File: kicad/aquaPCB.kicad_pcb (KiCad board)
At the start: 2 copper layers, 100 x 100 mm, 149 parts, among them J1 12V IN, J11 SSR G17, J12 SSR G22, J13 SSR G23, J14 SSR G27, J15 IN1, J16 IN2, J17 IN3, J18 IN4, J19 1-Wire 1, J2 Raspberry Pi, J22 I2C 1, J23 I2C 2, J24 Display, J25 pH probe, J26 Module, J27 AIN3, J4 OUT G18, J5 OUT G19, J6 OUT G12, J7 OUT G13, J8 OUT G16, J9 OUT G26, Q1 AOD4184A, Q10 AOD4185, Q2 AOD4184A, Q3 AOD4184A, Q4 AOD4184A, Q5 AOD4184A, Q6 AOD4184A, U1 TPS54360B, U2 AMS1117-3.3, U3 74HCT244D, U4 ULN2803A, U5 ADS1115IDGSR, U6 TLV9062IDR

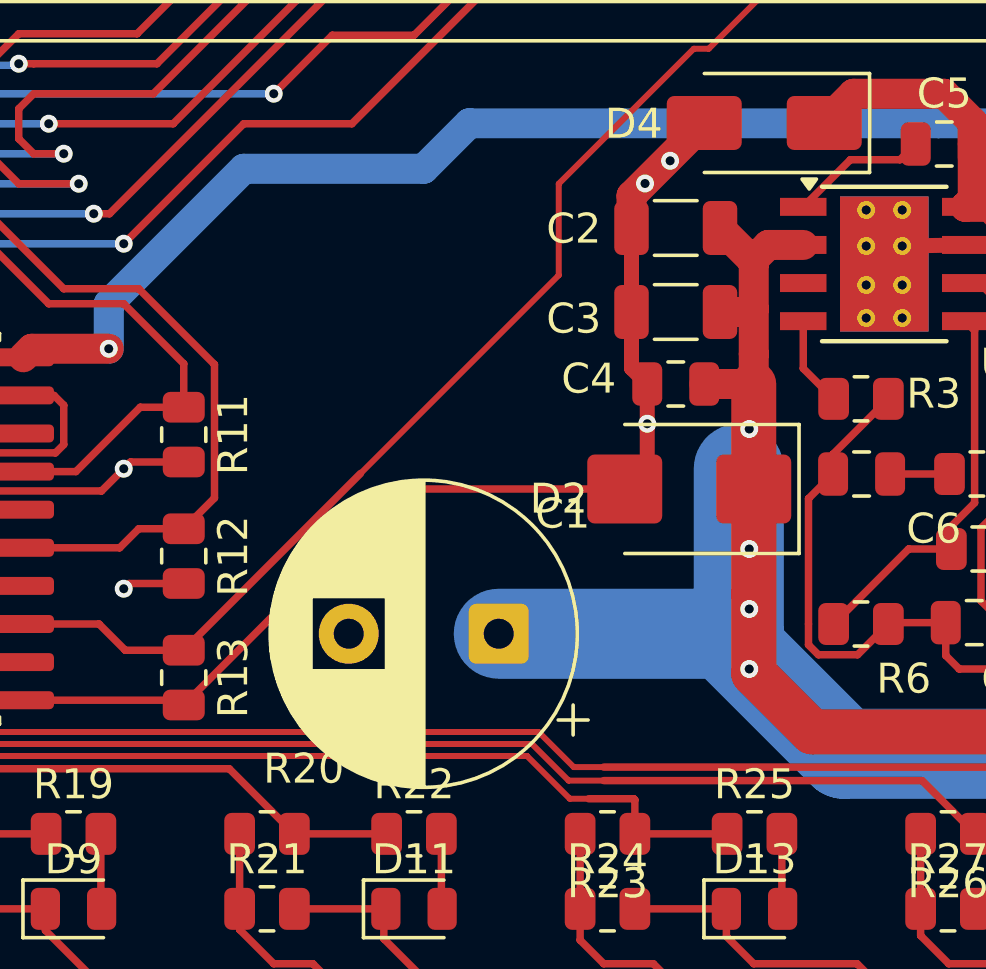
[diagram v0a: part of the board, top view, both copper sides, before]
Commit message: kicad: routing progress (by hand)
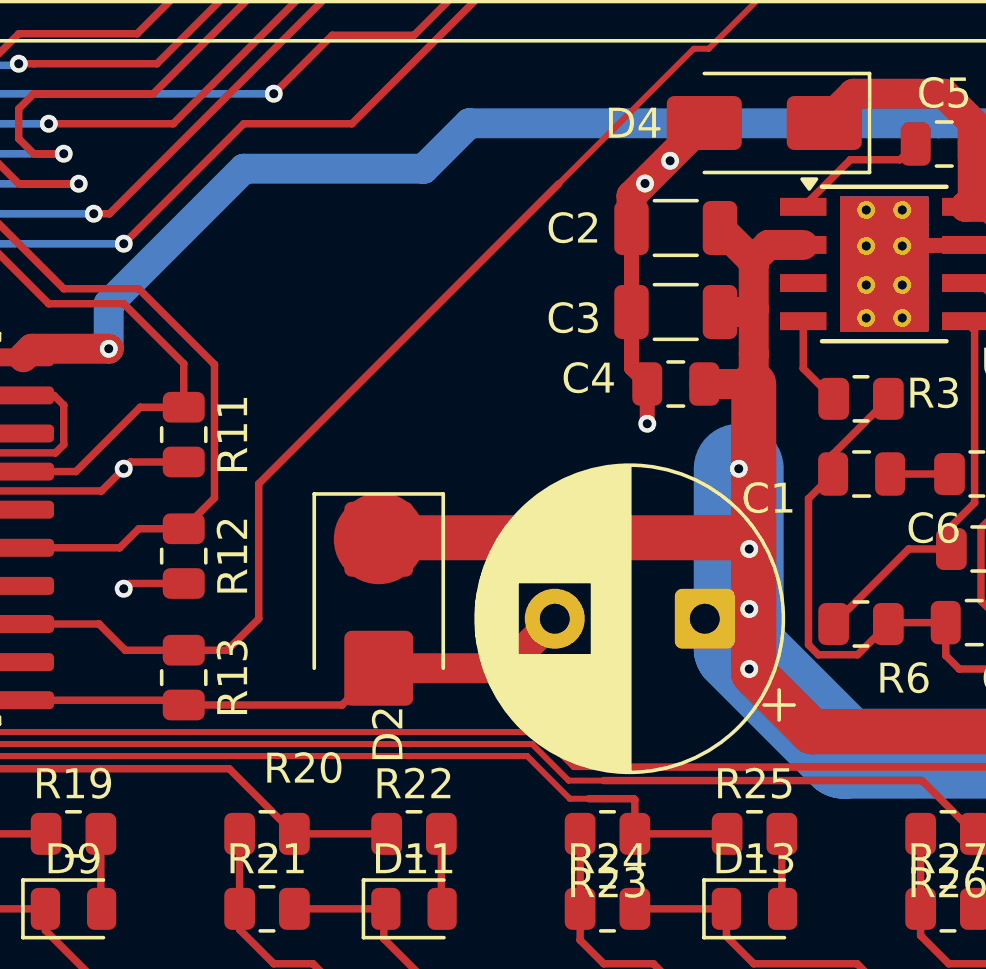
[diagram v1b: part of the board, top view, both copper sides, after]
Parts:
- moved D2 11.0 mm to (127.5, 98.5), turned to -90 degrees
- moved C1 6.89 mm to (138.4, 99.0)
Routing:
- net GND: track 441.3 -> 434.6 mm
- net VIN: track 365.2 -> 369.6 mm
- net GPIO18_Q1: track 37.6 -> 38.4 mm
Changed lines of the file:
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@@
 	(footprint "Diode_SMD:D_SMB"
 		(layer "F.Cu")
-		(at 137.85 94.675 180)
+		(at 127.5 98.5 -90)
 		(descr "Diode SMB (DO-214AA)")
 		(tags "Diode SMB (DO-214AA)")
 		(property "Reference" "D2"
-			(at 4.35 -0.325 0)
+			(at 4.35 -0.325 90)
 			(layer "F.SilkS")
 			(effects
@@
 		)
 		(property "Value" "SMBJ33A"
-			(at 0 3.1 0)
+			(at 0 3.1 90)
 			(layer "F.Fab")
 			(effects
@@
 		)
 		(property "Datasheet" ""
-			(at 0 0 180)
+			(at 0 0 270)
 			(unlocked yes)
 			(layer "F.Fab")
@@
 		)
 		(property "Description" "Zener diode"
-			(at 0 0 180)
+			(at 0 0 270)
 			(unlocked yes)
 			(layer "F.Fab")
@@
 		)
 		(property "LCSC" "C78419"
-			(at 0 0 180)
+			(at 0 0 270)
 			(unlocked yes)
 			(layer "F.Fab")
@@
 		(fp_line
 			(start -3.66 -2.15)
-			(end 2.15 -2.15)
+			(end -3.66 2.15)
 			(stroke
 				(width 0.12)
@@
 		(fp_line
 			(start -3.66 -2.15)
-			(end -3.66 2.15)
+			(end 2.15 -2.15)
 			(stroke
 				(width 0.12)
@@
 		)
 		(fp_line
-			(start 3.65 2.25)
-			(end -3.65 2.25)
+			(start -3.65 2.25)
+			(end -3.65 -2.25)
 			(stroke
 				(width 0.05)
@@
 		)
 		(fp_line
-			(start 3.65 -2.25)
-			(end 3.65 2.25)
+			(start 3.65 2.25)
+			(end -3.65 2.25)
 			(stroke
 				(width 0.05)
@@
 		)
 		(fp_line
-			(start -3.65 2.25)
-			(end -3.65 -2.25)
+			(start -3.65 -2.25)
+			(end 3.65 -2.25)
 			(stroke
 				(width 0.05)
@@
 		)
 		(fp_line
-			(start -3.65 -2.25)
-			(end 3.65 -2.25)
+			(start 3.65 -2.25)
+			(end 3.65 2.25)
 			(stroke
 				(width 0.05)
@@
 		)
 		(fp_line
-			(start 2.3 2)
-			(end -2.3 2)
+			(start -2.3 2)
+			(end -2.3 -2)
 			(stroke
 				(width 0.1)
@@
 		)
 		(fp_line
-			(start 2.3 -2)
-			(end 2.3 2)
+			(start 2.3 2)
+			(end -2.3 2)
 			(stroke
 				(width 0.1)
@@
 		)
 		(fp_line
-			(start 2.3 -2)
-			(end -2.3 -2)
+			(start 0.50118 0.75032)
+			(end 0.50118 -0.79908)
 			(stroke
 				(width 0.1)
@@
 		)
 		(fp_line
-			(start 0.50118 0.75032)
-			(end 0.50118 -0.79908)
+			(start -0.64944 0.00102)
+			(end 0.50118 0.75032)
 			(stroke
 				(width 0.1)
@@
 		)
 		(fp_line
-			(start 0.50118 0.00102)
-			(end 1.4994 0.00102)
+			(start -0.64944 0.00102)
+			(end -1.55114 0.00102)
 			(stroke
 				(width 0.1)
@@
 		(fp_line
 			(start -0.64944 0.00102)
-			(end 0.50118 0.75032)
+			(end 0.50118 -0.79908)
 			(stroke
 				(width 0.1)
@@
 		)
 		(fp_line
-			(start -0.64944 0.00102)
-			(end 0.50118 -0.79908)
+			(start 0.50118 0.00102)
+			(end 1.4994 0.00102)
 			(stroke
 				(width 0.1)
@@
 		)
 		(fp_line
-			(start -0.64944 0.00102)
-			(end -1.55114 0.00102)
+			(start -0.64944 -0.79908)
+			(end -0.64944 0.80112)
 			(stroke
 				(width 0.1)
@@
 		)
 		(fp_line
-			(start -0.64944 -0.79908)
-			(end -0.64944 0.80112)
+			(start 2.3 -2)
+			(end 2.3 2)
 			(stroke
 				(width 0.1)
@@
 		)
 		(fp_line
-			(start -2.3 2)
+			(start 2.3 -2)
 			(end -2.3 -2)
 			(stroke
@@
 		)
 		(fp_text user "${REFERENCE}"
-			(at 0 -3 0)
+			(at 0 -3 90)
 			(layer "F.Fab")
 			(effects
@@
 		)
 		(pad "1" smd roundrect
-			(at -2.15 0 180)
+			(at -2.15 0 270)
 			(size 2.5 2.3)
 			(layers "F.Cu" "F.Mask" "F.Paste")
@@
 		)
 		(pad "2" smd roundrect
-			(at 2.15 0 180)
+			(at 2.15 0 270)
 			(size 2.5 2.3)
 			(layers "F.Cu" "F.Mask" "F.Paste")
@@
 	(footprint "Capacitor_THT:CP_Radial_D10.0mm_P5.00mm"
 		(layer "F.Cu")
-		(at 131.5 99.5 180)
+		(at 138.367677 99 180)
 		(descr "CP, Radial series, Radial, pin pitch=5.00mm, diameter=10mm, height=16mm, Electrolytic Capacitor")
 		(tags "CP Radial series Radial pin pitch 5.00mm diameter 10mm height 16mm Electrolytic Capacitor")
@@
 	)
 	(segment
-		(start 136.45 93.925)
-		(end 135.7 94.675)
-		(width 0.5)
-		(layer "F.Cu")
-		(net "GND")
-	)
-	(segment
 		(start 150.7951 51.675)
 		(end 152.1 50.3701)
@@
 	)
 	(segment
+		(start 127.5 100.65)
+		(end 131.717677 100.65)
+		(width 1)
+		(layer "F.Cu")
+		(net "GND")
+	)
+	(segment
 		(start 125.4076 51.245)
 		(end 126.35 50.3026)
@@
 	)
 	(segment
+		(start 131.717677 100.65)
+		(end 133.367677 99)
+		(width 1)
+		(layer "F.Cu")
+		(net "GND")
+	)
+	(segment
 		(start 150.4375 109.9375)
 		(end 151.5 111)
@@
 	)
 	(segment
-		(start 106.35 90.285)
-		(end 104.715 90.285)
+		(start 126.275 101.875)
+		(end 127.5 100.65)
 		(width 0.25)
 		(layer "F.Cu")
@@
 	)
 	(segment
-		(start 163.5 111)
-		(end 163.5 114)
+		(start 106.35 90.285)
+		(end 104.715 90.285)
 		(width 0.25)
 		(layer "F.Cu")
@@
 	)
 	(segment
-		(start 136.45 92.5)
-		(end 136.45 93.925)
-		(width 0.5)
+		(start 163.5 111)
+		(end 163.5 114)
+		(width 0.25)
 		(layer "F.Cu")
 		(net "GND")
@@
 	)
 	(segment
-		(start 128.2 94.675)
-		(end 135.7 94.675)
-		(width 0.25)
-		(layer "F.Cu")
-		(net "GND")
-	)
-	(segment
-		(start 121 101.875)
-		(end 128.2 94.675)
-		(width 0.25)
-		(layer "F.Cu")
-		(net "GND")
-	)
-	(segment
 		(start 114.3 94.465908)
 		(end 114.574092 94.74)
@@
 	)
 	(segment
+		(start 121 101.875)
+		(end 126.275 101.875)
+		(width 0.25)
+		(layer "F.Cu")
+		(net "GND")
+	)
+	(segment
 		(start 145.814999 112.87)
 		(end 147 112.87)
@@
 	)
 	(segment
+		(start 127.55 96.3)
+		(end 139.8 96.3)
+		(width 1.5)
+		(layer "F.Cu")
+		(net "VIN")
+	)
+	(segment
 		(start 139.774999 127.93)
 		(end 142.494999 125.21)
@@
 	)
 	(segment
+		(start 127.5 96.35)
+		(end 127.55 96.3)
+		(width 3)
+		(layer "F.Cu")
+		(net "VIN")
+	)
+	(segment
 		(start 105.725 128.248377)
 		(end 105.725 127.93)
@@
 	)
 	(segment
-		(start 140 94.675)
+		(start 140 96.5)
 		(end 140 98.175)
 		(width 1.5)
@@
 	)
 	(segment
+		(start 140 94.675)
+		(end 140 96.5)
+		(width 1.5)
+		(layer "F.Cu")
+		(net "VIN")
+	)
+	(segment
 		(start 140 90.175)
 		(end 140 91.175)
@@
 	)
 	(via
-		(at 97.35 126.175)
+		(at 139.5 94)
 		(size 0.6)
 		(drill 0.3)
@@
 	)
 	(via
-		(at 139.85 100.675)
+		(at 97.35 126.175)
 		(size 0.6)
 		(drill 0.3)
@@
 	)
 	(via
-		(at 139.85 96.675)
+		(at 139.85 100.675)
 		(size 0.6)
 		(drill 0.3)
@@
 	)
 	(via
-		(at 98.85 124.73)
+		(at 139.85 96.675)
 		(size 0.6)
 		(drill 0.3)
@@
 	)
 	(via
-		(at 139.85 92.675)
+		(at 98.85 124.73)
 		(size 0.6)
 		(drill 0.3)
@@
 	)
 	(segment
-		(start 131.5 99.5)
-		(end 139.5 99.5)
-		(width 3)
-		(layer "B.Cu")
-		(net "VIN")
-	)
-	(segment
 		(start 117.075 127.93)
 		(end 117.075 132.98)
@@
 	)
 	(segment
+		(start 122.45 100.05)
+		(end 123.5 99)
+		(width 0.25)
+		(layer "F.Cu")
+		(net "GPIO18_Q1")
+	)
+	(segment
 		(start 118.175 99.175)
 		(end 115.65 99.175)
@@
 	(segment
 		(start 121 100.05)
-		(end 126.892677 94.157323)
+		(end 119.05 100.05)
 		(width 0.25)
 		(layer "F.Cu")
@@
 	(segment
 		(start 121 100.05)
-		(end 119.05 100.05)
+		(end 122.45 100.05)
 		(width 0.25)
 		(layer "F.Cu")
@@
 	)
 	(segment
-		(start 138.5 80)
-		(end 138 80)
-		(width 0.2)
+		(start 123.5 99)
+		(end 123.5 94.5)
+		(width 0.25)
 		(layer "F.Cu")
 		(net "GPIO18_Q1")
 	)
 	(segment
-		(start 133.5 87.55)
-		(end 126.892677 94.157323)
+		(start 138.5 80)
+		(end 138 80)
 		(width 0.2)
 		(layer "F.Cu")
@@
 	)
 	(segment
-		(start 133.5 84.5)
-		(end 133.5 87.55)
-		(width 0.2)
+		(start 123.5 94.5)
+		(end 133.5 84.5)
+		(width 0.25)
 		(layer "F.Cu")
 		(net "GPIO18_Q1")
